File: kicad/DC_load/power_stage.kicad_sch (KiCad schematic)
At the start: 57 parts, among them J2 red_terminal, J3 red terminal, J4 black terminal, J5 black terminal, Q3 FQP19N20C, Q4 FQP19N20C, Q5 FQP19N20C, Q6 FQP19N20C, U13 TLV9062, U3 NCS21802, U4 NCS21802, U5 TLV9062, U6 TLV9062, U7 LMT84LPM

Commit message: Oa.
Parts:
- R29, R32: LCSC (none) -> C22935
- R30, R33: value 50k -> 49.9k; LCSC (none) -> C23184
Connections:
- net GND: now also U13.5 (+)
- net at U13.6 (-): now also U13.7
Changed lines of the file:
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@@
 	(wire
 		(pts
+			(xy 242.57 149.86) (xy 240.03 149.86)
+		)
+		(stroke
+			(width 0)
+			(type default)
+		)
+	)
+	(wire
+		(pts
 			(xy 147.32 81.28) (xy 158.75 81.28)
 		)
@@
 	(wire
 		(pts
+			(xy 222.25 152.4) (xy 224.79 152.4)
+		)
+		(stroke
+			(width 0)
+			(type default)
+		)
+	)
+	(wire
+		(pts
 			(xy 125.73 177.8) (xy 125.73 182.88)
 		)
@@
 	(wire
 		(pts
+			(xy 222.25 152.4) (xy 222.25 157.48)
+		)
+		(stroke
+			(width 0)
+			(type default)
+		)
+	)
+	(wire
+		(pts
 			(xy 48.26 86.36) (xy 36.83 86.36)
 		)
@@
 	(wire
 		(pts
+			(xy 222.25 157.48) (xy 242.57 157.48)
+		)
+		(stroke
+			(width 0)
+			(type default)
+		)
+	)
+	(wire
+		(pts
 			(xy 36.83 86.36) (xy 36.83 81.28)
 		)
@@
 	(wire
 		(pts
+			(xy 242.57 157.48) (xy 242.57 149.86)
+		)
+		(stroke
+			(width 0)
+			(type default)
+		)
+	)
+	(wire
+		(pts
 			(xy 114.3 82.55) (xy 114.3 80.01)
 		)
@@
 			)
 		)
-		(property "LCSC" ""
+		(property "LCSC" "C22935"
 			(at 226.06 43.18 0)
 			(effects
@@
 			)
 		)
-		(property "LCSC" ""
+		(property "LCSC" "C22935"
 			(at 226.06 38.1 0)
 			(effects
@@
 			)
 		)
-		(property "Value" "50k"
-			(at 234.442 53.086 0)
+		(property "Value" "49.9k"
+			(at 232.664 53.086 0)
 			(effects
 				(font
@@
 			)
 		)
-		(property "LCSC" ""
+		(property "LCSC" "C23184"
 			(at 237.49 52.07 0)
 			(effects
@@
 		(dnp no)
 		(property "Reference" "R33"
-			(at 242.062 29.21 90)
+			(at 241.046 29.21 90)
 			(effects
 				(font
@@
 			)
 		)
-		(property "Value" "50k"
-			(at 251.46 29.21 90)
+		(property "Value" "49.9k"
+			(at 252.476 29.21 90)
 			(effects
 				(font
@@
 			)
 		)
-		(property "LCSC" ""
+		(property "LCSC" "C23184"
 			(at 246.38 30.48 0)
 			(effects
@@
 					(unit 1)
 				)
+			)
+		)
+	)
+	(symbol
+		(lib_id "power:GND")
+		(at 224.79 147.32 270)
+		(unit 1)
+		(exclude_from_sim no)
+		(in_bom yes)
+		(on_board yes)
+		(dnp no)
+		(fields_autoplaced yes)
+		(property "Reference" "#PWR0108"
+			(at 218.44 147.32 0)
+			(effects
+				(font
+					(size 1.27 1.27)
+				)
+				(hide yes)
+			)
+		)
+		(property "Value" "GND"
+			(at 220.98 147.3199 90)
+			(effects
+				(font
+					(size 1.27 1.27)
+				)
+				(justify right)
+			)
+		)
+		(property "Footprint" ""
+			(at 224.79 147.32 0)
+			(effects
+				(font
+					(size 1.27 1.27)
+				)
+				(hide yes)
+			)
+		)
+		(property "Datasheet" ""
+			(at 224.79 147.32 0)
+			(effects
+				(font
+					(size 1.27 1.27)
+				)
+				(hide yes)
+			)
+		)
+		(property "Description" "Power symbol creates a global label with name \"GND\" , ground"
+			(at 224.79 147.32 0)
+			(effects
+				(font
+					(size 1.27 1.27)
+				)
+				(hide yes)
+			)
+		)
+		(pin "1"
+		)
+		(instances
+			(project "DC_load"
+				(path "/ce255642-b081-42cc-af02-07a78c62b42e/6d7f5b85-3e99-49f9-8c4c-aaf8053997e0"
+					(reference "#PWR0108")
+					(unit 1)
+				)

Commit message: Most routing done.
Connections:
- net +5V is gone; now on net 5V: C8.1, U7.1 (+V_{S})
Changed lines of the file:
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@@
 			)
 		)
-		(property "Value" "+5V"
+		(property "Value" "5V"
 			(at 217.17 83.82 0)
 			(effects
@@
 			)
 		)
-		(property "Value" "+5V"
+		(property "Value" "5V"
 			(at 241.3 87.63 0)
 			(effects

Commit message: All cool
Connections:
- net SW_TEMP renamed SINK_TEMP
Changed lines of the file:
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@@
-		)
-	)
-	(global_label "SW_TEMP"
-		(shape output)
-		(at 204.47 96.52 180)
-		(fields_autoplaced yes)
-		(effects
-			(font
-				(size 1.27 1.27)
-			)
-			(justify right)
-		)
-		(property "Intersheetrefs" "${INTERSHEET_REFS}"
-			(at 193.0183 96.52 0)
-			(effects
-				(font
-					(size 1.27 1.27)
-				)
-				(justify right)
-				(hide yes)
-			)
 		)
 	)
@@
 		)
 	)
+	(hierarchical_label "SINK_TEMP"
+		(shape output)
+		(at 204.47 96.52 180)
+		(effects
+			(font
+				(size 1.27 1.27)
+			)
+			(justify right)
+		)
+	)

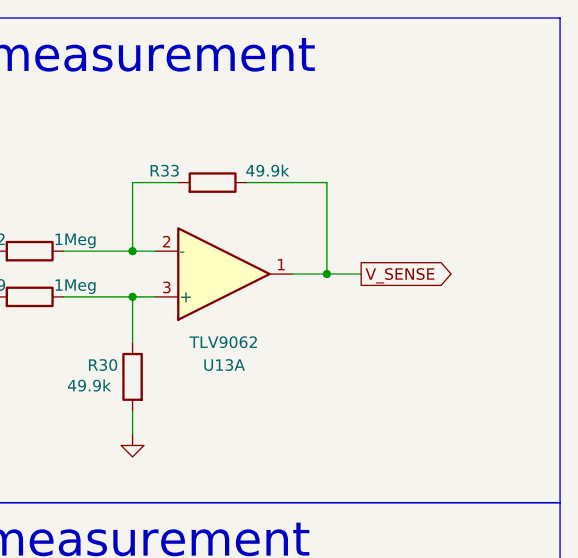
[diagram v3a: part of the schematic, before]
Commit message: Added voltage sense
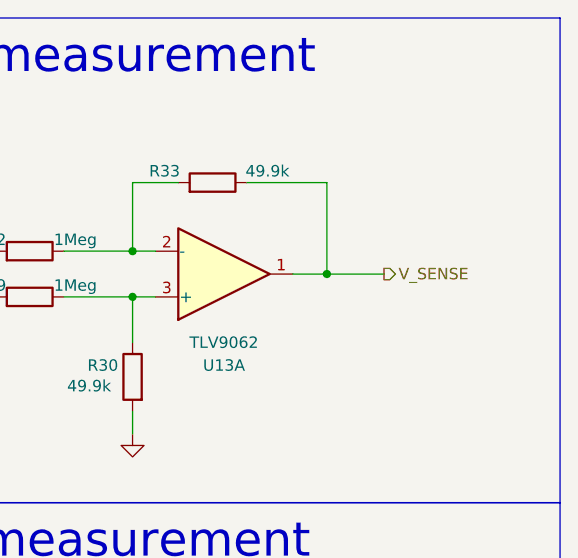
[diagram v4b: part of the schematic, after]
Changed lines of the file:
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@@
 	(wire
 		(pts
-			(xy 262.89 40.64) (xy 259.08 40.64)
+			(xy 259.08 40.64) (xy 265.43 40.64)
 		)
 		(stroke
@@
 		)
 	)
-	(global_label "V_SENSE"
-		(shape output)
-		(at 262.89 40.64 0)
-		(fields_autoplaced yes)
-		(effects
-			(font
-				(size 1.27 1.27)
-			)
-			(justify left)
-		)
-		(property "Intersheetrefs" "${INTERSHEET_REFS}"
-			(at 273.9789 40.64 0)
-			(effects
-				(font
-					(size 1.27 1.27)
-				)
-				(justify left)
-				(hide yes)
-			)
-		)
-	)
 	(hierarchical_label "CH1_MEAS"
 		(shape output)
@@
 		(effects
 			(font
+				(size 1.27 1.27)
+			)
+			(justify left)
+		)
+	)
+	(hierarchical_label "V_SENSE"
+		(shape output)
+		(at 265.43 40.64 0)
+		(effects
+			(font

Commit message: Done.
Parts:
- added TP10, TP8, TP9: TestPoint, TestPoint:TestPoint_Pad_D2.0mm, symbol Connector:TestPoint
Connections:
- net CH1_CONTROL: now also TP10.1
- net CH1_MEAS: now also TP9.1
- net GND: now also TP8.1

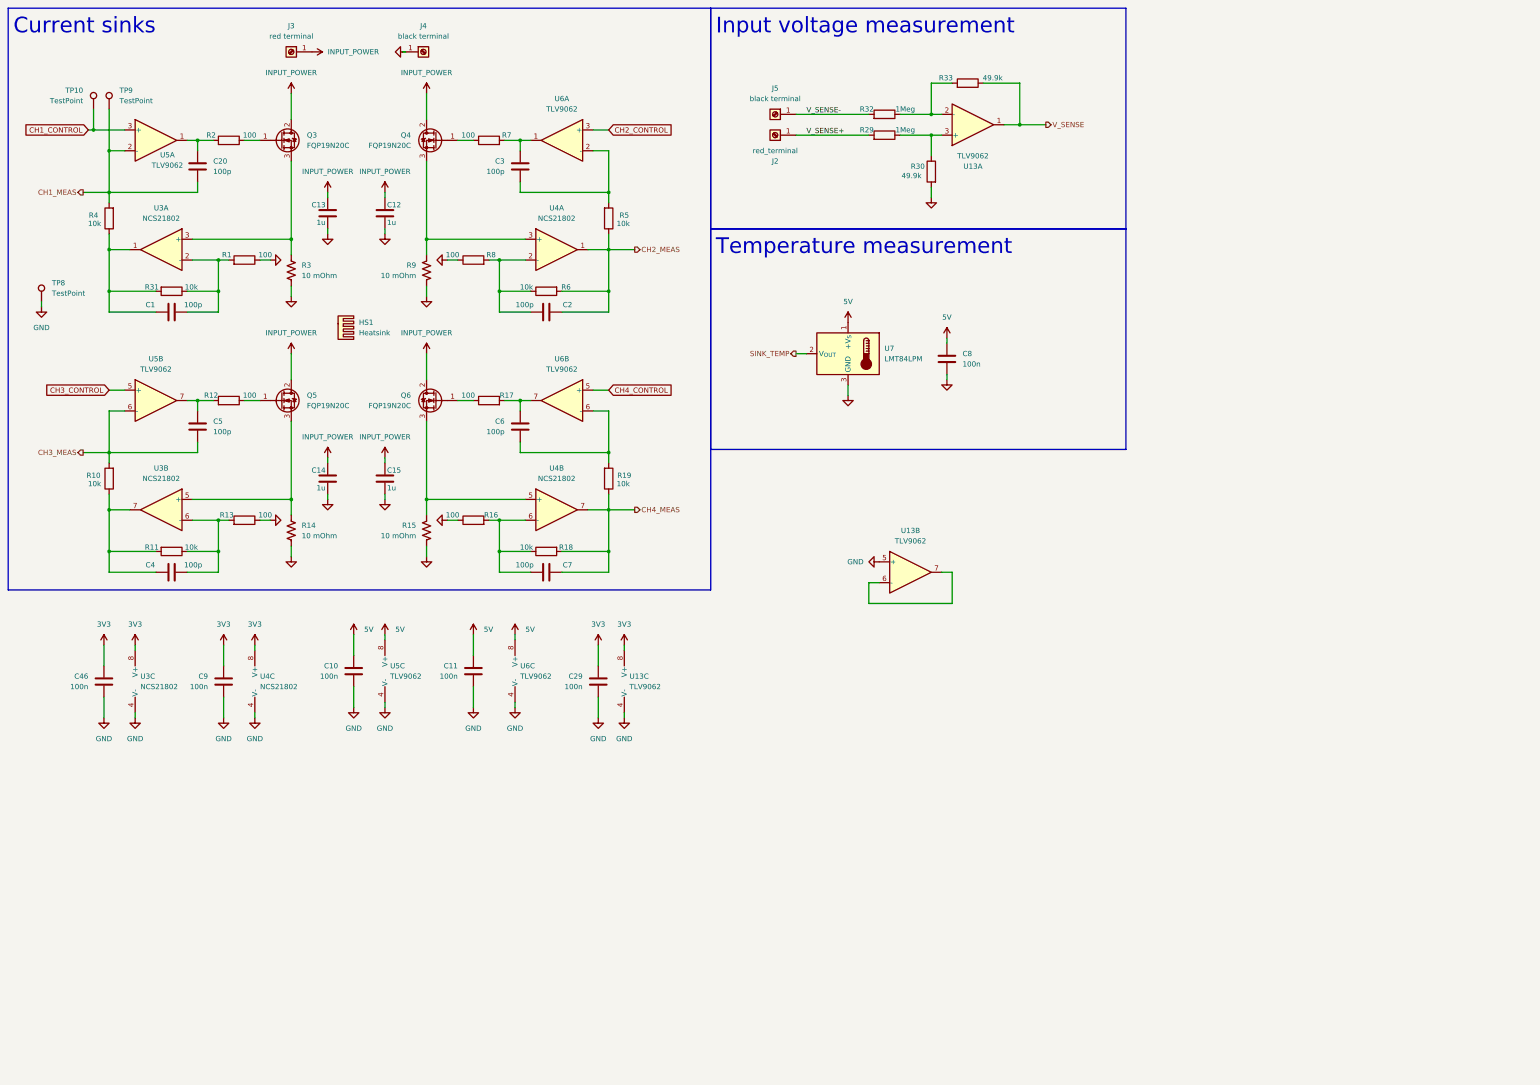
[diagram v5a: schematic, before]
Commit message: Vbe multiplier, constant current source 12V mosfet gate driver. RC filters moved lower. INA181 for 20x gain, 50 mOhm shunts. Jumper moved to BNC. Rough placement initiated.
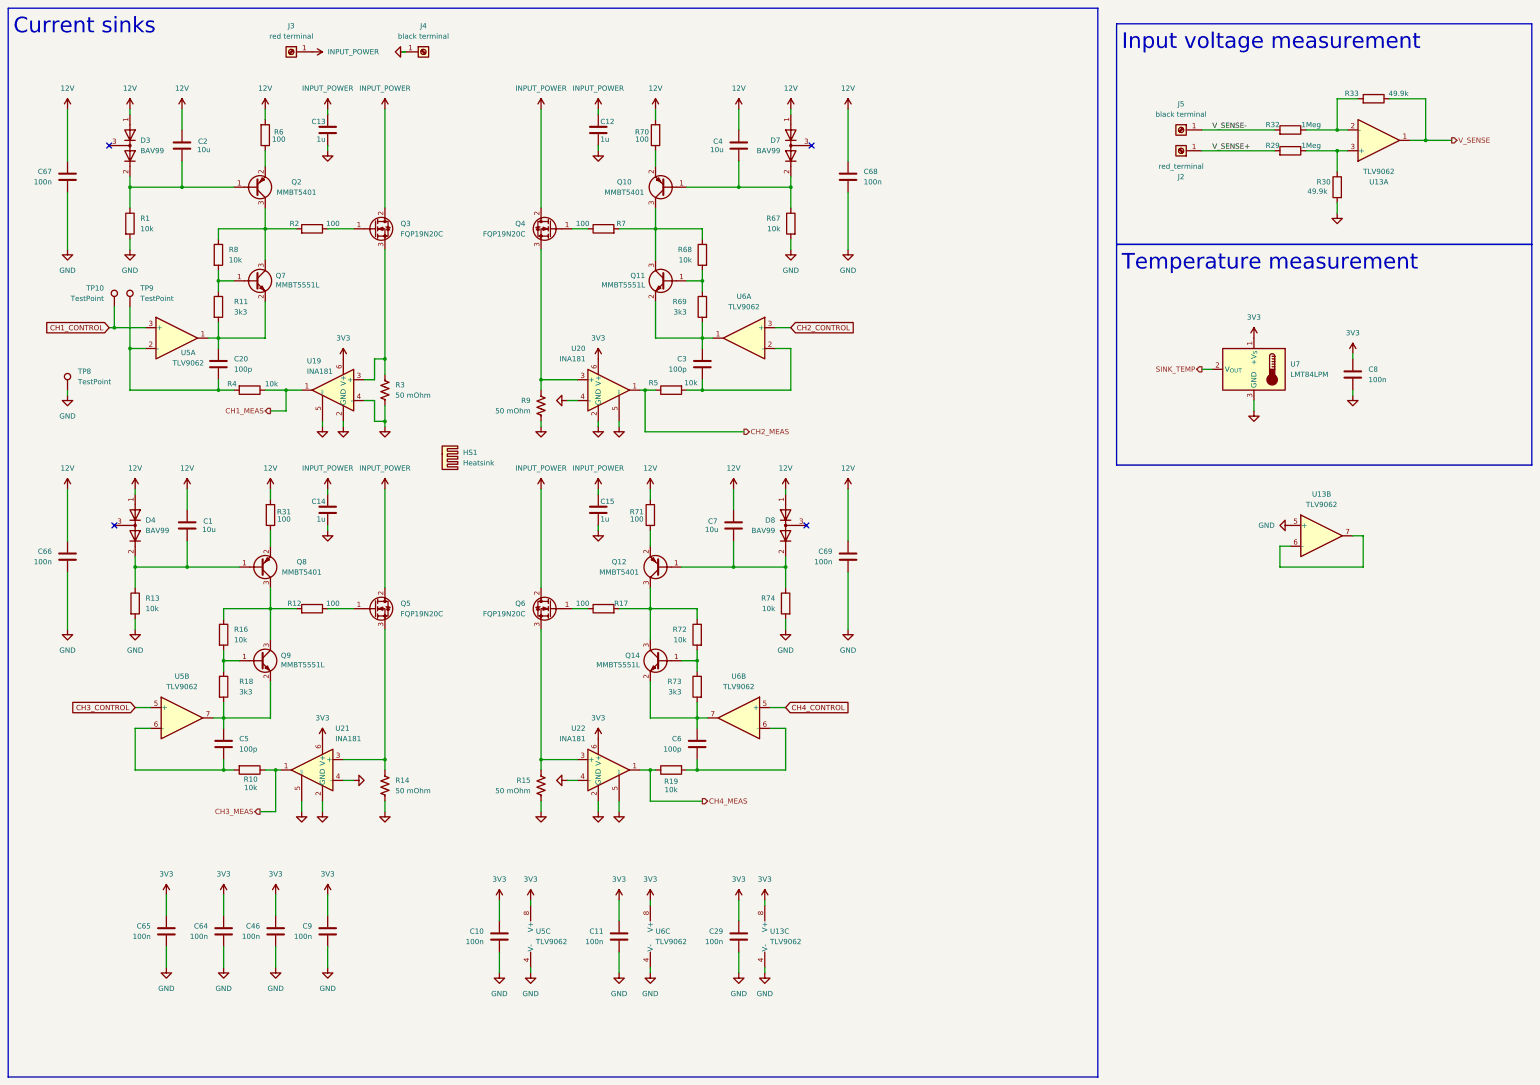
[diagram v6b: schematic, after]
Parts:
- removed U3, U4: NCS21802, Package_SO:OnSemi_Micro8, symbol Amplifier_Operational:TLV9062
- added C64, C65, C66, C67, C68, C69: 100n, Capacitor_SMD:C_0603_1608Metric_Pad1.08x0.95mm_HandSolder, symbol Device:C
- added D3, D4, D7, D8: BAV99, Package_TO_SOT_SMD:SOT-23, symbol Diode:BAV99
- added Q10, Q12, Q2, Q8: MMBT5401, Package_TO_SOT_SMD:SOT-23, symbol Transistor_BJT:MMBT3906
- added Q11, Q14, Q7, Q9: MMBT5551L, Package_TO_SOT_SMD:SOT-23, symbol Transistor_BJT:MMBT5551L
- added R67, R68, R72, R74: 10k, Resistor_SMD:R_0603_1608Metric_Pad0.98x0.95mm_HandSolder, symbol Device:R
- added R69, R73: 3k3, Resistor_SMD:R_0603_1608Metric_Pad0.98x0.95mm_HandSolder, symbol Device:R
- added R70, R71: 100, Resistor_SMD:R_0603_1608Metric_Pad0.98x0.95mm_HandSolder, symbol Device:R
- added U19, U20, U21, U22: INA181, Package_TO_SOT_SMD:SOT-23-6, symbol Amplifier_Current:INA181
- C1, C2, C4, C7: value 100p -> 10u; LCSC C14858 -> C96446
- R1, R13, R16, R8: value 100 -> 10k; LCSC C22775 -> C25804
- R11, R18: value 10k -> 3k3; LCSC C25804 -> C22978
- R14, R15, R3, R9: value 10 mOhm -> 50 mOhm
- R31, R6: value 10k -> 100; LCSC C25804 -> C22775
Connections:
- net 5V is gone; now on net 3V3: C10.2, C11.2, C8.1, U5.8 (V+), U6.8 (V+), U7.1 (+V_{S})
- net 3V3: now also C64.2, C65.2, U19.6 (V+), U20.6 (V+), U21.6 (V+), U22.6 (V+)
- net CH1_MEAS: now also R4.1, U19.1; no longer C20.1, R4.2, TP9.1, U5.2 (-)
- net CH2_MEAS: now also U20.1; no longer C2.1, R6.2
- net CH3_MEAS: now also R10.1, U21.1; no longer C5.1, R10.2, U5.6 (-)
- net CH4_MEAS: now also U22.1; no longer C7.1, R18.2
- net GND: now also R1.2, R13.2, C64.1, C65.1, C66.1, C67.1, C68.1, C69.1, R67.2, R74.2, U19.2 (GND), U19.4 (-), U19.5 (REF), U20.2 (GND), U20.4 (-), U20.5 (REF), U21.2 (GND), U21.4 (-), U21.5 (REF), U22.2 (GND), U22.4 (-), U22.5 (REF); no longer R1.1, R13.1, R16.1, R8.1
- net at Q6.3 (S), R15.1: now also U22.3 (+)
- net at R16.2, R18.1: now also Q9.1 (B); no longer C7.2
- net at Q3.3 (S), R3.1: now also U19.3 (+)
- net 12V: now reaches C1.1, R31.2
- net 12V: now also C2.1, C4.1, C7.1, R6.2, C66.2, C67.2, C68.2, C69.2, D3.1 (K), D4.1 (K), D7.1 (K), D8.1 (K), R70.2, R71.2; no longer R4.1
- net at C20.2, U5.1: now also R11.2, Q7.2 (E); no longer R2.2
- net at C3.2, U6.1: now also Q11.2 (E), R69.2; no longer R7.2
- net at Q4.3 (S), R9.1: now also U20.3 (+)
- net at Q5.3 (S), R14.1: now also U21.3 (+)
- net at C5.2, U5.7: now also R18.2, Q9.2 (E); no longer R12.2
- net at C6.2, U6.7: now also Q14.2 (E), R73.2; no longer R17.2
- new net: C2.2, D3.2 (A), Q2.1 (B), R1.1
- new net: Q2.2 (E), R6.1
- new net: Q2.3 (C), Q7.3 (C), R2.2, R8.1
- new net: Q11.1 (B), R68.2, R69.1
- new net: Q14.1 (B), R72.2, R73.1
- new net: Q12.3 (C), Q14.3 (C), R17.2, R72.1
- new net: C4.2, D7.2 (A), Q10.1 (B), R67.1
- new net: Q10.2 (E), R70.1
- new net: Q10.3 (C), Q11.3 (C), R68.1, R7.2
- new net: Q8.2 (E), R31.1
- new net: C7.2, D8.2 (A), Q12.1 (B), R74.1
- new net: C1.2, D4.2 (A), Q8.1 (B), R13.1
- new net: Q12.2 (E), R71.1
- new net: Q7.1 (B), R11.1, R8.2
- new net: Q8.3 (C), Q9.3 (C), R12.2, R16.1
- new net: C5.1, R10.2, U5.6 (-)
- new net: C20.1, R4.2, TP9.1, U5.2 (-)
- no-connect marks 0 -> 4
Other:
- moved on the sheet: C10, C11, C12, C13, C14, C15, C20, C29, C3, C5, C6, C8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

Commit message: Još gate driver layout.
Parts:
- removed TP10: TestPoint, TestPoint:TestPoint_Pad_D2.0mm, symbol Connector:TestPoint
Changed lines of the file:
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@@
 	)
 	(junction
-		(at 38.1 90.17)
-		(diameter 0)
-		(color 0 0 0 0)
-	)
-	(junction
 		(at 77.47 198.12)
 		(diameter 0)
@@
 	(wire
 		(pts
-			(xy 38.1 90.17) (xy 45.72 90.17)
+			(xy 36.83 90.17) (xy 45.72 90.17)
 		)
 		(stroke
@@
 	(wire
 		(pts
-			(xy 36.83 90.17) (xy 38.1 90.17)
-		)
-		(stroke
-			(width 0)
-			(type default)
-		)
-	)
-	(wire
-		(pts
 			(xy 64.77 161.29) (xy 64.77 158.75)
 		)
@@
 	(wire
 		(pts
-			(xy 38.1 85.09) (xy 38.1 90.17)
-		)
-		(stroke
-			(width 0)
-			(type default)
-		)
-	)
-	(wire
-		(pts
 			(xy 55.88 129.54) (xy 55.88 134.62)
 		)
@@
 					(unit 1)
 				)
-			)
-		)
-	)
-	(symbol
-		(lib_id "Connector:TestPoint")
-		(at 38.1 85.09 0)
-		(mirror y)
-		(unit 1)
-		(exclude_from_sim no)
-		(in_bom yes)
-		(on_board yes)
-		(dnp no)
-		(property "Reference" "TP10"
-			(at 35.56 80.518 0)
-			(effects
-				(font
-					(size 1.27 1.27)
-				)
-				(justify left)
-			)
-		)
-		(property "Value" "TestPoint"
-			(at 35.56 83.058 0)
-			(effects
-				(font
-					(size 1.27 1.27)
-				)
-				(justify left)
-			)
-		)
-		(property "Footprint" "TestPoint:TestPoint_Pad_D2.0mm"
-			(at 33.02 85.09 0)
-			(effects
-				(font
-					(size 1.27 1.27)
-				)
-				(hide yes)
-			)
-		)
-		(property "Datasheet" "~"
-			(at 33.02 85.09 0)
-			(effects
-				(font
-					(size 1.27 1.27)
-				)
-				(hide yes)
-			)
-		)
-		(property "Description" ""
-			(at 38.1 85.09 0)
-			(effects
-				(font
-					(size 1.27 1.27)
-				)
-				(hide yes)
-			)
-		)
-		(pin "1"
-		)
-		(instances
-			(project "DC_load"
-				(path "/ce255642-b081-42cc-af02-07a78c62b42e/6d7f5b85-3e99-49f9-8c4c-aaf8053997e0"
-					(reference "TP10")
-					(unit 1)
-				)

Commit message: Done???.
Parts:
- added C74, C75: 1n, Capacitor_SMD:C_0603_1608Metric_Pad1.08x0.95mm_HandSolder, symbol Device:C
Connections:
- net GND: now also C74.1
- net V_SENSE: now also C75.1
- net at R29.1, R30.1, U13.3 (+): now also C74.2
- net at R32.1, R33.2, U13.2 (-): now also C75.2
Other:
- moved on the sheet: R29, R32, R33
